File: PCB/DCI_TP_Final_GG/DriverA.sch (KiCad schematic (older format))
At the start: 18 parts, among them J201 DRIVER A OUT, U201 A3967

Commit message: Agrego codigos de catalogo
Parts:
- C201, C202: Descripcion CAP 680PF 50V CERAMICO 0805 -> CAP CER 680PF 50V; digikey# (none) -> 399-8110-1-ND; manf (none) -> KEMET; manf# (none) -> C681F5GACTU
- J201: Descripcion (none) -> Terminal Block x 4 5MM PCB; digikey# (none) -> 277-1238-ND; manf (none) -> Phoenix Contact; manf# (none) -> 1729034
- R201, R202, R203, R204, R208: Descripcion (none) -> RES 10K OHM SMD 0805; digikey# (none) -> 311-10KARCT-ND; manf (none) -> Yageo; manf# (none) -> RC0805JR-0710KL
- R205: digikey# (none) -> 311-10KARCT-ND; manf (none) -> Yageo; manf# (none) -> RC0805JR-0710KL
- R206: Descripcion RES SMD 6.8K OHM 0805 -> RES 6.8K OHM SMD 0805; digikey# (none) -> 311-6.80KCRCT-ND; manf (none) -> Yageo; manf# (none) -> RC0805FR-076K8L
- R207: digikey# (none) -> 311-2.40KCRCT-ND; manf (none) -> Yageo; manf# (none) -> RC0805FR-072K4L
- R209: Descripcion Resistencia SMD 0805 1/4 w 1% -> RES .75 OHM 1/4W 1% 0805 SMD; digikey# (none) -> RCWE.75DCT-ND; manf (none) -> Vishay Dale; manf# (none) -> RCWE0805R750FKEA
- R210: digikey# (none) -> RCWE.75DCT-ND; manf (none) -> Vishay Dale; manf# (none) -> RCWE0805R750FKEA
- R211, R212: Descripcion RES 20K OHM 0805 -> RES 20K OHM SMD 0805; digikey# (none) -> 311-20.0KCRCT-ND; manf (none) -> Yageo; manf# (none) -> RC0805FR-0720KL
- RV201: #Fab TS53YJ103MR10 -> (none); Descripcion (none) -> Potenciometro 10k SMD 5050; Digikey TS53YJ-10KTR-ND -> (none); digikey# (none) -> TS53YJ-10KTR-ND; manf (none) -> Vishay; manf# (none) -> TS53YJ103MR10
- U201: Descripcion (none) -> Stepper Driver A3967; digikey# (none) -> 620-1140-1-ND; manf (none) -> Allegro MicroSystems; manf# (none) -> A3967SLBTR-T
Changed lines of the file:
@@
 Title "Replica Dual EasyDriver v4.5"
 Date "2019-10-02"
-Rev ""
+Rev "Matias Brignone"
 Comp "Gonzalo Gontad - CESE-FIUBA"
 Comment1 ""
@@
 F 2 "Package_SO:SOIC-24W_7.5x15.4mm_P1.27mm" V 6100 -1300 50  0001 C CNN
 F 3 "https://github.com/cese-dci/tp-dci--Gonzalogontad/blob/master/info/A3967-Datasheet.pdf" H 5800 -1150 50  0001 C CNN
+F 4 "Stepper Driver A3967" H 3250 1150 50  0001 C CNN "Descripcion"
+F 5 "620-1140-1-ND" H 3250 1150 50  0001 C CNN "digikey#"
+F 6 "Allegro MicroSystems" H 3250 1150 50  0001 C CNN "manf"
+F 7 "A3967SLBTR-T" H 3250 1150 50  0001 C CNN "manf#"
 	1    3250 1150
 	1    0    0    -1
@@
 F 2 "TerminalBlock_Phoenix:TerminalBlock_Phoenix_MKDS-1,5-4_1x04_P5.00mm_Horizontal" H 8600 3600 50  0001 C CNN
 F 3 "~" H 8600 3600 50  0001 C CNN
+F 4 "Terminal Block x 4  5MM PCB" H 8600 3600 50  0001 C CNN "Descripcion"
+F 5 "277-1238-ND" H 8600 3600 50  0001 C CNN "digikey#"
+F 6 "Phoenix Contact" H 8600 3600 50  0001 C CNN "manf"
+F 7 "1729034" H 8600 3600 50  0001 C CNN "manf#"
 	1    8600 3600
 	1    0    0    -1
@@
 F 2 "Resistor_SMD:R_0805_2012Metric" V 6830 3400 50  0001 C CNN
 F 3 "" H 6900 3400 50  0001 C CNN
-F 4 "Resistencia SMD 0805 1/4 w 1%" V 6900 3400 50  0001 C CNN "Descripcion"
+F 4 "RES .75 OHM 1/4W 1% 0805 SMD" V 6900 3400 50  0001 C CNN "Descripcion"
+F 5 "RCWE.75DCT-ND" H 6900 3400 50  0001 C CNN "digikey#"
+F 6 "Vishay Dale" H 6900 3400 50  0001 C CNN "manf"
+F 7 "RCWE0805R750FKEA" H 6900 3400 50  0001 C CNN "manf#"
 	1    6900 3400
 	0    1    1    0
@@
 F 3 "" H 6900 4400 50  0001 C CNN
 F 4 "RES .75 OHM 1/4W 1% 0805 SMD" V 6900 4400 50  0001 C CNN "Descripcion"
+F 5 "RCWE.75DCT-ND" H 6900 4400 50  0001 C CNN "digikey#"
+F 6 "Vishay Dale" H 6900 4400 50  0001 C CNN "manf"
+F 7 "RCWE0805R750FKEA" H 6900 4400 50  0001 C CNN "manf#"
 	1    6900 4400
 	0    1    1    0
@@
 F 2 "Resistor_SMD:R_0805_2012Metric" V 6980 5200 50  0001 C CNN
 F 3 "" H 7050 5200 50  0001 C CNN
-F 4 "RES 20K OHM 0805" H 7050 5200 50  0001 C CNN "Descripcion"
+F 4 "RES 20K OHM SMD 0805" H 7050 5200 50  0001 C CNN "Descripcion"
+F 5 "311-20.0KCRCT-ND" H 7050 5200 50  0001 C CNN "digikey#"
+F 6 "Yageo" H 7050 5200 50  0001 C CNN "manf"
+F 7 "RC0805FR-0720KL" H 7050 5200 50  0001 C CNN "manf#"
 	1    7050 5200
 	1    0    0    -1
@@
 F 2 "Capacitor_SMD:C_0805_2012Metric" H 7488 5050 50  0001 C CNN
 F 3 "" H 7450 5200 50  0001 C CNN
-F 4 "CAP 680PF 50V CERAMICO 0805" H 7450 5200 50  0001 C CNN "Descripcion"
+F 4 "CAP CER 680PF 50V " H 7450 5200 50  0001 C CNN "Descripcion"
+F 5 "399-8110-1-ND" H 7450 5200 50  0001 C CNN "digikey#"
+F 6 "KEMET" H 7450 5200 50  0001 C CNN "manf"
+F 7 "C681F5GACTU" H 7450 5200 50  0001 C CNN "manf#"
 	1    7450 5200
 	1    0    0    -1
@@
 F 2 "Resistor_SMD:R_0805_2012Metric" V 6980 2550 50  0001 C CNN
 F 3 "" H 7050 2550 50  0001 C CNN
-F 4 "RES 20K OHM 0805" H 7050 2550 50  0001 C CNN "Descripcion"
+F 4 "RES 20K OHM SMD 0805" H 7050 2550 50  0001 C CNN "Descripcion"
+F 5 "311-20.0KCRCT-ND" H 7050 2550 50  0001 C CNN "digikey#"
+F 6 "Yageo" H 7050 2550 50  0001 C CNN "manf"
+F 7 "RC0805FR-0720KL" H 7050 2550 50  0001 C CNN "manf#"
 	1    7050 2550
 	1    0    0    -1
@@
 F 2 "Capacitor_SMD:C_0805_2012Metric" H 7488 2400 50  0001 C CNN
 F 3 "" H 7450 2550 50  0001 C CNN
-F 4 "CAP 680PF 50V CERAMICO 0805" H 7450 2550 50  0001 C CNN "Descripcion"
+F 4 "CAP CER 680PF 50V " H 7450 2550 50  0001 C CNN "Descripcion"
+F 5 "399-8110-1-ND" H 7450 2550 50  0001 C CNN "digikey#"
+F 6 "KEMET" H 7450 2550 50  0001 C CNN "manf"
+F 7 "C681F5GACTU" H 7450 2550 50  0001 C CNN "manf#"
 	1    7450 2550
 	1    0    0    -1
@@
 F 2 "Resistor_SMD:R_0805_2012Metric" V 4180 2550 50  0001 C CNN
 F 3 "" H 4250 2550 50  0001 C CNN
-F 4 "RES SMD 6.8K OHM 0805" H 4250 2550 50  0001 C CNN "Descripcion"
+F 4 "RES  6.8K OHM SMD 0805" H 4250 2550 50  0001 C CNN "Descripcion"
+F 5 "311-6.80KCRCT-ND" H 4250 2550 50  0001 C CNN "digikey#"
+F 6 "Yageo" H 4250 2550 50  0001 C CNN "manf"
+F 7 "RC0805FR-076K8L" H 4250 2550 50  0001 C CNN "manf#"
 	1    4250 2550
 	1    0    0    -1
@@
 F 3 "" H 4250 2050 50  0001 C CNN
 F 4 "RES 10K OHM SMD 0805" H 4250 2050 50  0001 C CNN "Descripcion"
+F 5 "311-10KARCT-ND" H 4250 2050 50  0001 C CNN "digikey#"
+F 6 "Yageo" H 4250 2050 50  0001 C CNN "manf"
+F 7 "RC0805JR-0710KL" H 4250 2050 50  0001 C CNN "manf#"
 	1    4250 2050
 	1    0    0    -1
@@
 F 2 "Potentiometer_SMD:Potentiometer_Vishay_TS53YJ_Vertical" H 4300 4950 50  0001 C CNN
 F 3 "" H 4300 4950 50  0001 C CNN
-F 4 "TS53YJ-10KTR-ND" H 4300 4950 50  0001 C CNN "Digikey"
-F 5 "TS53YJ103MR10" H 4300 4950 50  0001 C CNN "#Fab"
+F 4 "TS53YJ-10KTR-ND" H 4300 4950 50  0001 C CNN "digikey#"
+F 5 "TS53YJ103MR10" H 4300 4950 50  0001 C CNN "manf#"
+F 6 "Potenciometro 10k SMD 5050" H 4300 4950 50  0001 C CNN "Descripcion"
+F 7 "Vishay" H 4300 4950 50  0001 C CNN "manf"
 	1    4300 4950
 	1    0    0    -1
@@
 F 3 "" H 4300 5400 50  0001 C CNN
 F 4 "RES 2.4K OHM SMD 0805" H 4300 5400 50  0001 C CNN "Descripcion"
+F 5 "311-2.40KCRCT-ND" H 4300 5400 50  0001 C CNN "digikey#"
+F 6 "Yageo" H 4300 5400 50  0001 C CNN "manf"
+F 7 "RC0805FR-072K4L" H 4300 5400 50  0001 C CNN "manf#"
 	1    4300 5400
 	1    0    0    -1
@@
 F 2 "Resistor_SMD:R_0805_2012Metric" V 4430 3650 50  0001 C CNN
 F 3 "" H 4500 3650 50  0001 C CNN
+F 4 "RES 10K OHM SMD 0805" H 4500 3650 50  0001 C CNN "Descripcion"
+F 5 "311-10KARCT-ND" H 4500 3650 50  0001 C CNN "digikey#"
+F 6 "Yageo" H 4500 3650 50  0001 C CNN "manf"
+F 7 "RC0805JR-0710KL" H 4500 3650 50  0001 C CNN "manf#"
 	1    4500 3650
 	0    1    1    0
@@
 F 2 "Resistor_SMD:R_0805_2012Metric" V 3930 3500 50  0001 C CNN
 F 3 "" H 4000 3500 50  0001 C CNN
+F 4 "RES 10K OHM SMD 0805" H 4000 3500 50  0001 C CNN "Descripcion"
+F 5 "311-10KARCT-ND" H 4000 3500 50  0001 C CNN "digikey#"
+F 6 "Yageo" H 4000 3500 50  0001 C CNN "manf"
+F 7 "RC0805JR-0710KL" H 4000 3500 50  0001 C CNN "manf#"
 	1    4000 3500
 	0    1    1    0
@@
 F 2 "Resistor_SMD:R_0805_2012Metric" V 3930 3350 50  0001 C CNN
 F 3 "" H 4000 3350 50  0001 C CNN
+F 4 "RES 10K OHM SMD 0805" H 4000 3350 50  0001 C CNN "Descripcion"
+F 5 "311-10KARCT-ND" H 4000 3350 50  0001 C CNN "digikey#"
+F 6 "Yageo" H 4000 3350 50  0001 C CNN "manf"
+F 7 "RC0805JR-0710KL" H 4000 3350 50  0001 C CNN "manf#"
 	1    4000 3350
 	0    1    1    0
@@
 F 2 "Resistor_SMD:R_0805_2012Metric" V 3930 4000 50  0001 C CNN
 F 3 "" H 4000 4000 50  0001 C CNN
+F 4 "RES 10K OHM SMD 0805" H 4000 4000 50  0001 C CNN "Descripcion"
+F 5 "311-10KARCT-ND" H 4000 4000 50  0001 C CNN "digikey#"
+F 6 "Yageo" H 4000 4000 50  0001 C CNN "manf"
+F 7 "RC0805JR-0710KL" H 4000 4000 50  0001 C CNN "manf#"
 	1    4000 4000
 	0    1    1    0
@@
 F 2 "Resistor_SMD:R_0805_2012Metric" V 3930 4250 50  0001 C CNN
 F 3 "" H 4000 4250 50  0001 C CNN
+F 4 "RES 10K OHM SMD 0805" H 4000 4250 50  0001 C CNN "Descripcion"
+F 5 "311-10KARCT-ND" H 4000 4250 50  0001 C CNN "digikey#"
+F 6 "Yageo" H 4000 4250 50  0001 C CNN "manf"
+F 7 "RC0805JR-0710KL" H 4000 4250 50  0001 C CNN "manf#"
 	1    4000 4250
 	0    1    1    0

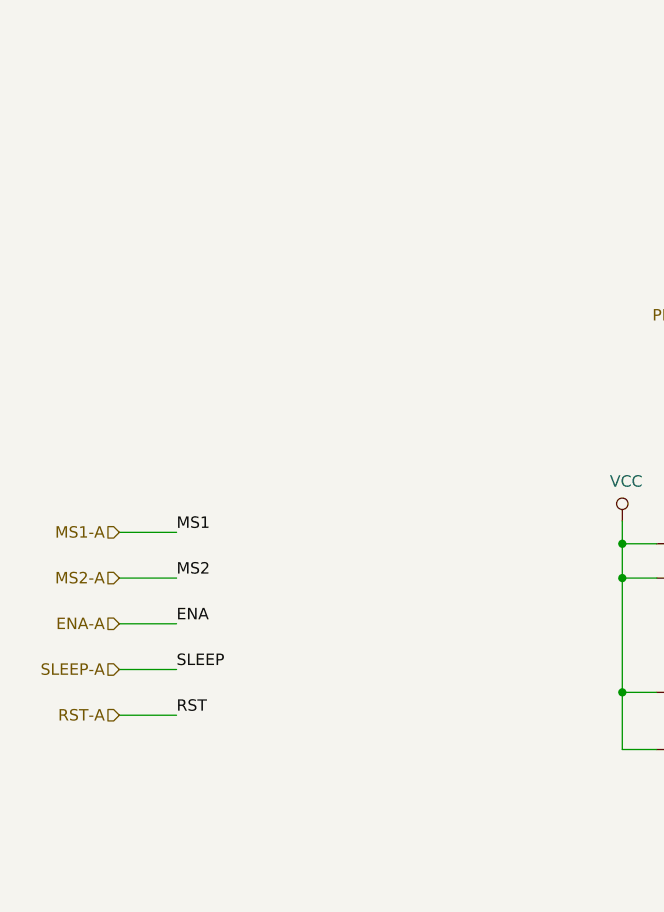
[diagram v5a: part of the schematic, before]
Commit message: Cambio de ubicacion de capacitores de desacople en la jerarquia del esquematico y actualizacion de identificadores en PCB
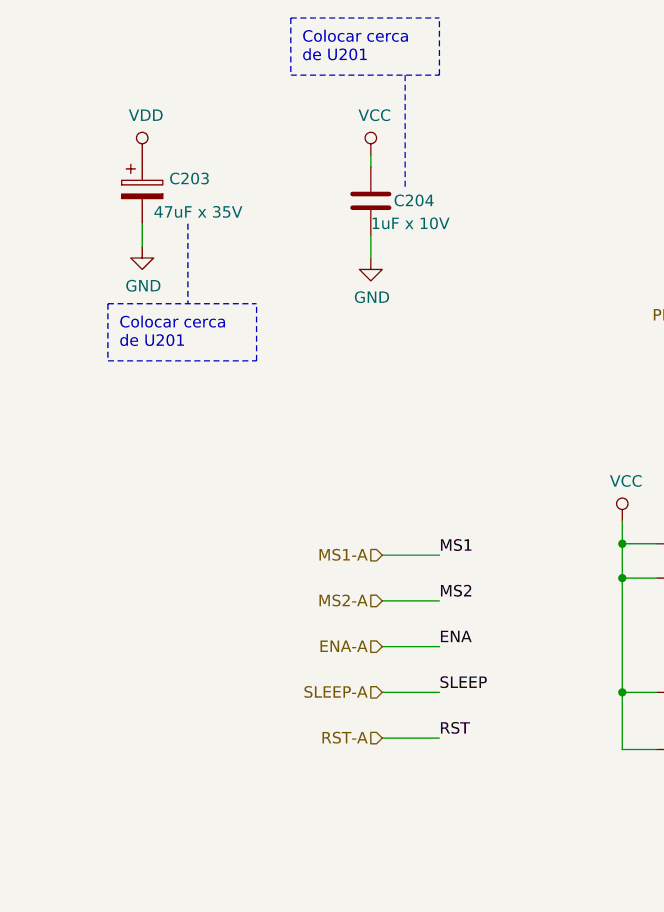
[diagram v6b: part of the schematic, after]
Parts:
- added C203: 47uF x 35V, Capacitor_THT:CP_Radial_D5.0mm_P2.00mm, symbol Device:CP
- added C204: 1uF x 10V, Capacitor_SMD:C_0805_2012Metric, symbol Device:C
- U201: footprint Package_SO:SOIC-24W_7.5x15.4mm_P1.27mm -> DCI_TP_Final_GG:SOIC-24W_7.5x15.4mm_P1.27mm
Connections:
- net GND: now also C203.2, C204.2
- net VCC: now also C204.1
- net VDD: now also C203.1
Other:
- note added: "Colocar cerca\nde U201"
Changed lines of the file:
@@
 Sheet 2 4
 Title "Replica Dual EasyDriver v4.5"
-Date "2019-10-02"
-Rev "Matias Brignone"
+Date "2019-10-26"
+Rev "M Brignone"
 Comp "Gonzalo Gontad - CESE-FIUBA"
-Comment1 ""
+Comment1 "Revisores: M. Ribelotta y M. Brignone"
 Comment2 ""
 Comment3 ""
@@
 F 0 "U201" H 5800 -1100 50  0000 C CNN
 F 1 "A3967" H 5800 -1250 50  0000 C CNN
-F 2 "Package_SO:SOIC-24W_7.5x15.4mm_P1.27mm" V 6100 -1300 50  0001 C CNN
+F 2 "DCI_TP_Final_GG:SOIC-24W_7.5x15.4mm_P1.27mm" V 6100 -1300 50  0001 C CNN
 F 3 "https://github.com/cese-dci/tp-dci--Gonzalogontad/blob/master/info/A3967-Datasheet.pdf" H 5800 -1150 50  0001 C CNN
 F 4 "Stepper Driver A3967" H 3250 1150 50  0001 C CNN "Descripcion"
@@
 Text Label 4500 4250 0    50   ~ 0
 RST
-Text HLabel 1500 3300 0    50   Input ~ 0
+Text HLabel 2650 3400 0    50   Input ~ 0
 MS1-A
-Text HLabel 1500 3500 0    50   Input ~ 0
+Text HLabel 2650 3600 0    50   Input ~ 0
 MS2-A
-Text HLabel 1500 3700 0    50   Input ~ 0
+Text HLabel 2650 3800 0    50   Input ~ 0
 ENA-A
-Text HLabel 1500 3900 0    50   Input ~ 0
+Text HLabel 2650 4000 0    50   Input ~ 0
 SLEEP-A
-Text HLabel 1500 4100 0    50   Input ~ 0
+Text HLabel 2650 4200 0    50   Input ~ 0
 RST-A
 Wire Wire Line
-	1750 3300 1500 3300
-Wire Wire Line
-	1750 3500 1500 3500
-Wire Wire Line
-	1750 3700 1500 3700
-Wire Wire Line
-	1750 3900 1500 3900
-Wire Wire Line
-	1750 4100 1500 4100
-Text Label 1750 3300 0    50   ~ 0
+	2900 3400 2650 3400
+Wire Wire Line
+	2900 3600 2650 3600
+Wire Wire Line
+	2900 3800 2650 3800
+Wire Wire Line
+	2900 4000 2650 4000
+Wire Wire Line
+	2900 4200 2650 4200
+Text Label 2900 3400 0    50   ~ 0
 MS1
-Text Label 1750 3500 0    50   ~ 0
+Text Label 2900 3600 0    50   ~ 0
 MS2
-Text Label 1750 3700 0    50   ~ 0
+Text Label 2900 3800 0    50   ~ 0
 ENA
-Text Label 1750 3900 0    50   ~ 0
+Text Label 2900 4000 0    50   ~ 0
 SLEEP
-Text Label 1750 4100 0    50   ~ 0
+Text Label 2900 4200 0    50   ~ 0
 RST
 Text Label 8150 3450 0    50   ~ 0
@@
 Text Notes 3000 6800 0    79   ~ 0
 TP201 = Ajuste de maxima corriente del motor\nPara Vref =5V -> Iout = 833mA\nPara Vref =2V -> Iout = 333mA\nPara Vref =1V -> Iout = 166mA
+$Comp
+L Device:CP C?
+U 1 1 5DB649DD
+P 1600 1800
+AR Path="/5D973A64/5DB649DD" Ref="C?"  Part="1"
+AR Path="/5D9739A6/5DB649DD" Ref="C203"  Part="1"
+F 0 "C203" H 1718 1846 50  0000 L CNN
+F 1 "47uF x 35V" H 1650 1700 50  0000 L CNN
+F 2 "Capacitor_THT:CP_Radial_D5.0mm_P2.00mm" H 1638 1650 50  0001 C CNN
+F 3 "https://ar.mouser.com/datasheet/2/293/e-ufw-1511690.pdf" H 1600 1800 50  0001 C CNN
+F 4 "CAP Electrolitico 47UF  35V RADIAL" H 1600 1800 50  0001 C CNN "Descripcion"
+F 5 "493-11044-1-ND" H 1600 1800 50  0001 C CNN "digikey#"
+F 6 "Nichicon" H 1600 1800 50  0001 C CNN "manf"
+F 7 "UFW1V470MDD1TD" H 1600 1800 50  0001 C CNN "manf#"
+	1    1600 1800
+	1    0    0    -1
+$EndComp
+$Comp
+L power:GND #PWR?
+U 1 1 5DB649E3
+P 1600 2050
+AR Path="/5D973A64/5DB649E3" Ref="#PWR?"  Part="1"
+AR Path="/5D9739A6/5DB649E3" Ref="#PWR0217"  Part="1"
+F 0 "#PWR0217" H 1600 1800 50  0001 C CNN
+F 1 "GND" H 1605 1877 50  0000 C CNN
+F 2 "" H 1600 2050 50  0001 C CNN
+F 3 "" H 1600 2050 50  0001 C CNN
+	1    1600 2050
+	1    0    0    -1
+$EndComp
+Wire Wire Line
+	1600 1950 1600 2050
+Text Notes 1500 2500 0    50   ~ 0
+Colocar cerca\nde U201
+Wire Notes Line
+	1800 1950 1800 2300
+Wire Notes Line
+	1450 2300 1450 2550
+Wire Notes Line
+	1450 2550 2100 2550
+Wire Notes Line
+	2100 2550 2100 2300
+Wire Notes Line
+	1450 2300 2100 2300
+$Comp
+L Device:C C?
+U 1 1 5DB70497
+P 2600 1850
+AR Path="/5D973A64/5DB70497" Ref="C?"  Part="1"
+AR Path="/5D9739A6/5DB70497" Ref="C204"  Part="1"
+F 0 "C204" H 2700 1850 50  0000 L CNN
+F 1 "1uF x 10V" H 2600 1750 50  0000 L CNN
+F 2 "Capacitor_SMD:C_0805_2012Metric" H 2638 1700 50  0001 C CNN
+F 3 "https://ar.mouser.com/datasheet/2/212/KEM_C1005_Y5V_SMD-1101305.pdf" H 2600 1850 50  0001 C CNN
+F 4 "CAP CER 1UF 10V " H 2600 1850 50  0001 C CNN "Descripcion"
+F 5 "399-1172-1-ND" H 2600 1850 50  0001 C CNN "digikey#"
+F 6 "KEMET" H 2600 1850 50  0001 C CNN "manf"
+F 7 "C0805C105K8RACTU" H 2600 1850 50  0001 C CNN "manf#"
+	1    2600 1850
+	1    0    0    -1
+$EndComp
+$Comp
+L power:GND #PWR?
+U 1 1 5DB7049D
+P 2600 2100
+AR Path="/5D973A64/5DB7049D" Ref="#PWR?"  Part="1"
+AR Path="/5D9739A6/5DB7049D" Ref="#PWR0219"  Part="1"
+F 0 "#PWR0219" H 2600 1850 50  0001 C CNN
+F 1 "GND" H 2605 1927 50  0000 C CNN
+F 2 "" H 2600 2100 50  0001 C CNN
+F 3 "" H 2600 2100 50  0001 C CNN
+	1    2600 2100
+	1    0    0    -1
+$EndComp
+Wire Wire Line
+	2600 2100 2600 2000
+Wire Wire Line
+	2600 1700 2600 1650
+Text Notes 2300 1250 0    50   ~ 0
+Colocar cerca\nde U201
+Wire Notes Line
+	2250 1300 2900 1300
+Wire Notes Line
+	2900 1300 2900 1050
+Wire Notes Line
+	2250 1050 2900 1050
+Wire Notes Line
+	2750 1300 2750 1800
+Wire Notes Line
+	2250 1050 2250 1300
+$Comp
+L power:VDD #PWR0216
+U 1 1 5DBCA68C
+P 1600 1650
+F 0 "#PWR0216" H 1600 1500 50  0001 C CNN
+F 1 "VDD" H 1617 1823 50  0000 C CNN
+F 2 "" H 1600 1650 50  0001 C CNN
+F 3 "" H 1600 1650 50  0001 C CNN
+	1    1600 1650
+	1    0    0    -1
+$EndComp
+$Comp
+L power:VCC #PWR0218
+U 1 1 5DBCAF58
+P 2600 1650
+F 0 "#PWR0218" H 2600 1500 50  0001 C CNN
+F 1 "VCC" H 2617 1823 50  0000 C CNN
+F 2 "" H 2600 1650 50  0001 C CNN
+F 3 "" H 2600 1650 50  0001 C CNN
+	1    2600 1650
+	1    0    0    -1
+$EndComp
 $EndSCHEMATC
